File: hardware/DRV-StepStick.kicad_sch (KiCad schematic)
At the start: 21 parts, among them J1 PCIe_Stepper, J2 Motor, J3 StepStickL, J4 StepStickR, J5 Conn_01x04, J6 SPI Mode, J7 Conn_01x02, U2 74LVC1G06

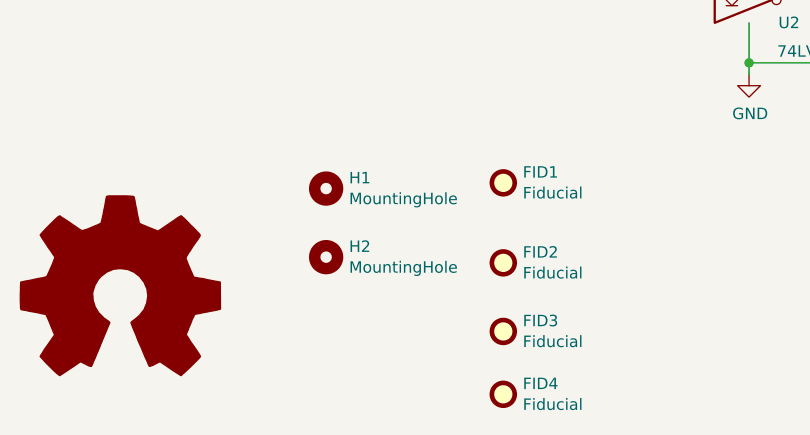
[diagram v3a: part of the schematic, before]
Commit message: Update of PCBs
- added tooling holes
- added order number location under components

Updated projects:
- DRV-Stepstick
- TMC2209
- TMC2130
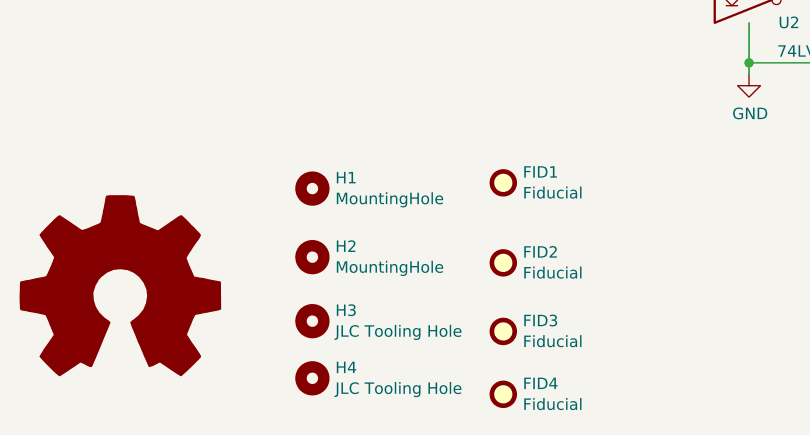
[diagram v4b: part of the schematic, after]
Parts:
- added H3, H4: JLC Tooling Hole, PrntrBoardV2:JLC_Tool_hole, symbol Mechanical:MountingHole
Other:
- moved on the sheet: H1, H2
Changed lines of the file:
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@@
     )
   )
-  (symbol (lib_id "Mechanical:MountingHole") (at 140.97 167.64 0) (unit 1)
-    (in_bom no) (on_board yes)
-    (property "Reference" "H1" (id 0) (at 143.51 166.4716 0)
-      (effects (font (size 1.27 1.27)) (justify left))
-    )
-    (property "Value" "MountingHole" (id 1) (at 143.51 168.783 0)
-      (effects (font (size 1.27 1.27)) (justify left))
-    )
-    (property "Footprint" "MountingHole:MountingHole_2.7mm_M2.5" (id 2) (at 140.97 167.64 0)
-      (effects (font (size 1.27 1.27)) hide)
-    )
-    (property "Datasheet" "~" (id 3) (at 140.97 167.64 0)
-      (effects (font (size 1.27 1.27)) hide)
-    )
-  )
-  (symbol (lib_id "Mechanical:MountingHole") (at 140.97 175.26 0) (unit 1)
-    (in_bom no) (on_board yes)
-    (property "Reference" "H2" (id 0) (at 143.51 174.0916 0)
-      (effects (font (size 1.27 1.27)) (justify left))
-    )
-    (property "Value" "MountingHole" (id 1) (at 143.51 176.403 0)
-      (effects (font (size 1.27 1.27)) (justify left))
-    )
-    (property "Footprint" "MountingHole:MountingHole_2.7mm_M2.5" (id 2) (at 140.97 175.26 0)
-      (effects (font (size 1.27 1.27)) hide)
-    )
-    (property "Datasheet" "~" (id 3) (at 140.97 175.26 0)
+  (symbol (lib_id "Mechanical:MountingHole") (at 139.446 167.64 0) (unit 1)
+    (in_bom no) (on_board yes)
+    (property "Reference" "H1" (id 0) (at 141.986 166.4716 0)
+      (effects (font (size 1.27 1.27)) (justify left))
+    )
+    (property "Value" "MountingHole" (id 1) (at 141.986 168.783 0)
+      (effects (font (size 1.27 1.27)) (justify left))
+    )
+    (property "Footprint" "MountingHole:MountingHole_2.7mm_M2.5" (id 2) (at 139.446 167.64 0)
+      (effects (font (size 1.27 1.27)) hide)
+    )
+    (property "Datasheet" "~" (id 3) (at 139.446 167.64 0)
+      (effects (font (size 1.27 1.27)) hide)
+    )
+  )
+  (symbol (lib_id "Mechanical:MountingHole") (at 139.446 175.26 0) (unit 1)
+    (in_bom no) (on_board yes)
+    (property "Reference" "H2" (id 0) (at 141.986 174.0916 0)
+      (effects (font (size 1.27 1.27)) (justify left))
+    )
+    (property "Value" "MountingHole" (id 1) (at 141.986 176.403 0)
+      (effects (font (size 1.27 1.27)) (justify left))
+    )
+    (property "Footprint" "MountingHole:MountingHole_2.7mm_M2.5" (id 2) (at 139.446 175.26 0)
+      (effects (font (size 1.27 1.27)) hide)
+    )
+    (property "Datasheet" "~" (id 3) (at 139.446 175.26 0)
+      (effects (font (size 1.27 1.27)) hide)
+    )
+  )
+  (symbol (lib_id "Mechanical:MountingHole") (at 139.446 182.372 0) (unit 1)
+    (in_bom no) (on_board yes)
+    (property "Reference" "H3" (id 0) (at 141.986 181.2036 0)
+      (effects (font (size 1.27 1.27)) (justify left))
+    )
+    (property "Value" "JLC Tooling Hole" (id 1) (at 141.986 183.515 0)
+      (effects (font (size 1.27 1.27)) (justify left))
+    )
+    (property "Footprint" "PrntrBoardV2:JLC_Tool_hole" (id 2) (at 139.446 182.372 0)
+      (effects (font (size 1.27 1.27)) hide)
+    )
+    (property "Datasheet" "~" (id 3) (at 139.446 182.372 0)
+      (effects (font (size 1.27 1.27)) hide)
+    )
+  )
+  (symbol (lib_id "Mechanical:MountingHole") (at 139.446 188.722 0) (unit 1)
+    (in_bom no) (on_board yes)
+    (property "Reference" "H4" (id 0) (at 141.986 187.5536 0)
+      (effects (font (size 1.27 1.27)) (justify left))
+    )
+    (property "Value" "JLC Tooling Hole" (id 1) (at 141.986 189.865 0)
+      (effects (font (size 1.27 1.27)) (justify left))
+    )
+    (property "Footprint" "PrntrBoardV2:JLC_Tool_hole" (id 2) (at 139.446 188.722 0)
+      (effects (font (size 1.27 1.27)) hide)
+    )
+    (property "Datasheet" "~" (id 3) (at 139.446 188.722 0)
       (effects (font (size 1.27 1.27)) hide)
     )
@@
       (reference "H2") (unit 1) (value "MountingHole") (footprint "MountingHole:MountingHole_2.7mm_M2.5")
     )
+    (path "/6d3c23dd-b2c8-49ab-94b9-3fe4fa1e1f2a"
+      (reference "H3") (unit 1) (value "JLC Tooling Hole") (footprint "PrntrBoardV2:JLC_Tool_hole")
+    )
+    (path "/c9ea6fdd-1e79-4138-86b3-37d166a4083b"
+      (reference "H4") (unit 1) (value "JLC Tooling Hole") (footprint "PrntrBoardV2:JLC_Tool_hole")
+    )
     (path "/00000000-0000-0000-0000-00005d91aa30"
